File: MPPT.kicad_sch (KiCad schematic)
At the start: 15 parts, among them U10 LTC3130

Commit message: v3.1 Updates
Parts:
- C10: renamed from C7; value 1uF -> 1u
- C11: renamed from C8; value 22nF -> 22n
- C12: renamed from C9; value 22nF -> 22n
- C13: renamed from C11; value 1uF -> 1u
- C14: renamed from C12; value 47uF -> 47u
- C15: renamed from C10; value 4.7uF -> 4u7
- C7: renamed from C4; value 47uF -> 47u
- C8: renamed from C5; value 10uF -> 10u
- C9: renamed from C6; value 1uF -> 1u
- L1: value 6.8uH -> 6.8u
- R52: renamed from R1; value 0R (DNI) -> 0R; now not fitted
- renumbered R2 to R53, R3 to R54, R4 to R55, U10 to U6
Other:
- company: (none) -> Carnegie Mellon University
- title: (none) -> Argus XY Solar Panel
- moved on the sheet: C13, C14

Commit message: Local Stash
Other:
- moved on the sheet: C10, C11, C12, C15, L1

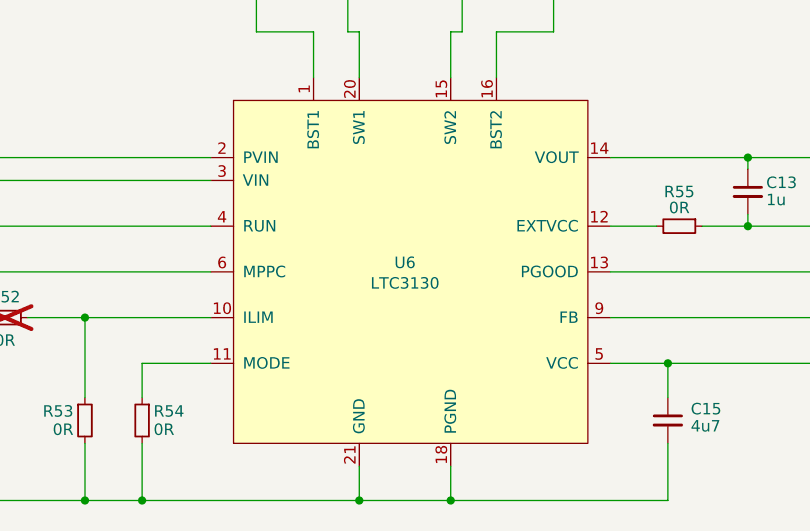
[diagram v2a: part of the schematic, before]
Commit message: Updated access port, added deployment sensor
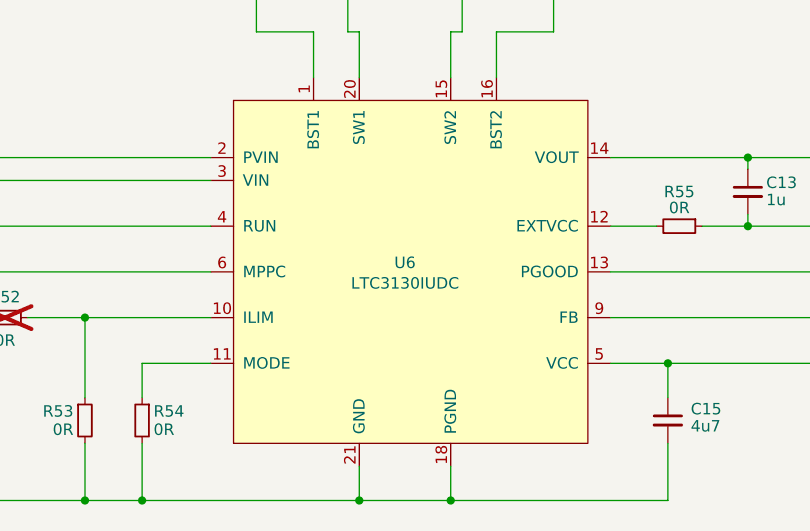
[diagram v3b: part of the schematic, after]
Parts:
- C10: MPN (none) -> C2214844; Mfr. # CL10B105KP8NFNC -> (none); Order https://www.digikey.com/product-detail/en/samsung-electro-m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 -> (none); Voltage 10V -> (none)
- C11, C12: MPN (none) -> C161234; Mfr. # GCM188R72A223KA37D -> (none); Order https://www.digikey.com/product-detail/en/murata-electronic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 -> (none); Voltage 100V -> (none)
- C13: MPN (none) -> C2214844; Mfr. # GRM32EC81C476KE15L -> (none); Order https://www.digikey.com/product-detail/en/murata-electronic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 -> (none); Voltage 16V -> (none)
- C15: MPN (none) -> C437575; Mfr. # C1608X7S1A475K080AC -> (none); Order https://www.digikey.com/product-detail/en/tdk-corporation/C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 -> (none); Voltage 10V -> (none)
- C8: MPN (none) -> C126617; Mfr. # C1608X7S1A475K080AC -> (none); Order https://www.digikey.com/product-detail/en/tdk-corporation/C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 -> (none); Voltage 10V -> (none)
- C9: MPN (none) -> C2214844; Mfr. # C1608X7S1A475K080AC -> (none); Order https://www.digikey.com/product-detail/en/tdk-corporation/C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 -> (none); Voltage 10V -> (none)
- R52: DNI (none) -> DNI; now left out of the parts list
- R53, R54, R55: MPN (none) -> C844915; Mfr. # RK73Z1JTTDr -> (none); Order https://www.digikey.com/product-detail/en/koa-speer-electro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 -> (none)
- U6: value LTC3130 -> LTC3130IUDC; MPN (none) -> C684244
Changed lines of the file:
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@@
 			)
 		)
-		(property "Mfr. #" "C1608X7S1A475K080AC"
+		(property "MPN" "C126617"
 			(at 68.58 96.52 0)
-			(effects
-				(font
-					(size 1.27 1.27)
-				)
-				(hide yes)
-			)
-		)
-		(property "Order" "https://www.digikey.com/product-detail/en/tdk-corporation/C1608X7S1A475K080AC/445-14258-1-ND/3955924"
-			(at 68.58 96.52 0)
-			(effects
-				(font
-					(size 1.27 1.27)
-				)
-				(hide yes)
-			)
-		)
-		(property "Voltage" "10V"
-			(at 73.025 99.06 0)
 			(effects
 				(font
@@
 			)
 		)
-		(property "Mfr. #" "GCM188R72A223KA37D"
+		(property "MPN" "C161234"
 			(at 165.1 68.58 90)
-			(effects
-				(font
-					(size 1.27 1.27)
-				)
-				(hide yes)
-			)
-		)
-		(property "Order" "https://www.digikey.com/product-detail/en/murata-electronics/GCM188R72A223KA37D/490-4782-1-ND/1641701"
-			(at 165.1 68.58 90)
-			(effects
-				(font
-					(size 1.27 1.27)
-				)
-				(hide yes)
-			)
-		)
-		(property "Voltage" "100V"
-			(at 165.1 71.755 90)
 			(effects
 				(font
@@
 			)
 		)
-		(property "Mfr. #" "RK73Z1JTTD\r"
-			(at 118.11 119.38 0)
-			(effects
-				(font
-					(size 1.27 1.27)
-				)
-				(hide yes)
-			)
-		)
-		(property "Order" "https://www.digikey.com/product-detail/en/koa-speer-electronics-inc/RK73Z1JTTD/2019-RK73Z1JTTDCT-ND/9847522\r"
+		(property "MPN" "C844915"
 			(at 118.11 119.38 0)
 			(effects
@@
 		(unit 1)
 		(exclude_from_sim no)
-		(in_bom yes)
+		(in_bom no)
 		(on_board yes)
 		(dnp yes)
@@
 			)
 		)
+		(property "DNI" "DNI"
+			(at 109.22 107.95 90)
+			(effects
+				(font
+					(size 1.27 1.27)
+				)
+				(hide yes)
+			)
+		)
 		(pin "1"
 		)
@@
 			)
 		)
-		(property "Mfr. #" "CL10B105KP8NFNC"
+		(property "MPN" "C2214844"
 			(at 88.9 96.52 0)
-			(effects
-				(font
-					(size 1.27 1.27)
-				)
-				(hide yes)
-			)
-		)
-		(property "Order" "https://www.digikey.com/product-detail/en/samsung-electro-mechanics/CL10B105KP8NFNC/1276-1945-1-ND/3890031"
-			(at 88.9 96.52 0)
-			(effects
-				(font
-					(size 1.27 1.27)
-				)
-				(hide yes)
-			)
-		)
-		(property "Voltage" "10V"
-			(at 93.345 99.06 0)
 			(effects
 				(font
@@
 			)
 		)
-		(property "Mfr. #" "GRM32EC81C476KE15L"
+		(property "MPN" "C2214844"
 			(at 191.77 93.98 0)
-			(effects
-				(font
-					(size 1.27 1.27)
-				)
-				(hide yes)
-			)
-		)
-		(property "Order" "https://www.digikey.com/product-detail/en/murata-electronics/GRM32EC81C476KE15L/490-10531-1-ND/5026469"
-			(at 191.77 93.98 0)
-			(effects
-				(font
-					(size 1.27 1.27)
-				)
-				(hide yes)
-			)
-		)
-		(property "Voltage" "16V"
-			(at 196.215 95.885 0)
 			(effects
 				(font
@@
 			)
 		)
-		(property "Value" "LTC3130"
+		(property "Value" "LTC3130IUDC"
 			(at 153.67 104.14 0)
 			(effects
@@
 		)
 		(property "Description" ""
+			(at 153.67 102.87 0)
+			(effects
+				(font
+					(size 1.27 1.27)
+				)
+				(hide yes)
+			)
+		)
+		(property "MPN" "C684244"
 			(at 153.67 102.87 0)
 			(effects
@@
 			)
 		)
-		(property "Mfr. #" "GCM188R72A223KA37D"
+		(property "MPN" "C161234"
 			(at 142.24 68.58 90)
-			(effects
-				(font
-					(size 1.27 1.27)
-				)
-				(hide yes)
-			)
-		)
-		(property "Order" "https://www.digikey.com/product-detail/en/murata-electronics/GCM188R72A223KA37D/490-4782-1-ND/1641701"
-			(at 142.24 68.58 90)
-			(effects
-				(font
-					(size 1.27 1.27)
-				)
-				(hide yes)
-			)
-		)
-		(property "Voltage" "100V"
-			(at 142.24 71.755 90)
 			(effects
 				(font
@@
 			)
 		)
-		(property "Mfr. #" "C1608X7S1A475K080AC"
+		(property "MPN" "C2214844"
 			(at 78.74 96.52 0)
-			(effects
-				(font
-					(size 1.27 1.27)
-				)
-				(hide yes)
-			)
-		)
-		(property "Order" "https://www.digikey.com/product-detail/en/tdk-corporation/C1608X7S1A475K080AC/445-14258-1-ND/3955924"
-			(at 78.74 96.52 0)
-			(effects
-				(font
-					(size 1.27 1.27)
-				)
-				(hide yes)
-			)
-		)
-		(property "Voltage" "10V"
-			(at 83.185 99.06 0)
 			(effects
 				(font
@@
 			)
 		)
-		(property "Mfr. #" "C1608X7S1A475K080AC"
+		(property "MPN" "C437575"
 			(at 182.88 119.38 0)
-			(effects
-				(font
-					(size 1.27 1.27)
-				)
-				(hide yes)
-			)
-		)
-		(property "Order" "https://www.digikey.com/product-detail/en/tdk-corporation/C1608X7S1A475K080AC/445-14258-1-ND/3955924"
-			(at 182.88 119.38 0)
-			(effects
-				(font
-					(size 1.27 1.27)
-				)
-				(hide yes)
-			)
-		)
-		(property "Voltage" "10V"
-			(at 187.325 121.92 0)
 			(effects
 				(font
@@
 			)
 		)
-		(property "Mfr. #" "RK73Z1JTTD\r"
-			(at 124.46 119.38 0)
-			(effects
-				(font
-					(size 1.27 1.27)
-				)
-				(hide yes)
-			)
-		)
-		(property "Order" "https://www.digikey.com/product-detail/en/koa-speer-electronics-inc/RK73Z1JTTD/2019-RK73Z1JTTDCT-ND/9847522\r"
+		(property "MPN" "C844915"
 			(at 124.46 119.38 0)
 			(effects
@@
 			)
 		)
-		(property "Mfr. #" "RK73Z1JTTD\r"
-			(at 184.15 97.79 0)
-			(effects
-				(font
-					(size 1.27 1.27)
-				)
-				(hide yes)
-			)
-		)
-		(property "Order" "https://www.digikey.com/product-detail/en/koa-speer-electronics-inc/RK73Z1JTTD/2019-RK73Z1JTTDCT-ND/9847522\r"
-			(at 184.15 97.79 0)
-			(effects
-				(font
+		(property "MPN" "C844915"
+			(at 184.15 97.79 90)
+			(effects
+				(font

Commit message: Local Stash
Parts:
- C10, C13, C9: MPN C2214844 -> C126592
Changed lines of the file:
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@@
 			)
 		)
-		(property "MPN" "C2214844"
+		(property "MPN" "C126592"
 			(at 88.9 96.52 0)
 			(effects
@@
 			)
 		)
-		(property "MPN" "C2214844"
+		(property "MPN" "C126592"
 			(at 191.77 93.98 0)
 			(effects
@@
 			)
 		)
-		(property "MPN" "C2214844"
+		(property "MPN" "C126592"
 			(at 78.74 96.52 0)
 			(effects
